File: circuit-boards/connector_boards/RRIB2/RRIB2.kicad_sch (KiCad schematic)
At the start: 90 parts, among them J1 DIO0, J10 DIO9, J11 DIO22, J12 DIO23, J13 DIO24, J14 DIO25, J15 RR_DIO0, J16 RR_DIO1, J17 RR_DIO2, J18 RR_DIO3, J19 RR_DIO4, J2 DIO1, J20 RR_DIO5, J21 RR_DIO6, J22 RR_DIO7, J23 RR_DIO8, J24 RR_DIO9, J25 ENC0, J26 ENC1, J27 ENC2, J28 ENC3, J29 ENC4, J3 DIO2, J30 ENC5, J31 ENC_AD0, J32 ENC_AD1, J33 ENC_AD2, J34 ENC_AD3, J35 ENC_AD4, J36 ENC_AD5, J37 RLY0, J38 RLY1, J39 RLY2, J4 DIO3, J40 RLY3, J41 AIN0, J42 AIN1, J43 AIN2, J44 AIN3, J45 AIN4, J46 AIN5, J47 AIN6, J48 AIN7, J49 RR_RELAY0, J5 DIO4, J50 RR_RELAY1, J51 RR_RELAY2, J52 RR_RELAY3, J53 RR_AIN0, J54 RR_AIN1, J55 RR_AIN2, J56 RR_AIN3, J57 PWM0, J58 PWM1, J59 PWM2, J6 DIO5, J60 PWM3, J61 PWM4, J62 PWM5, J63 PWM6, J64 PWM7, J65 PWM8, J66 PWM9, J67 RR_PWM0, J68 RR_PWM1, J69 RR_PWM2, J7 DIO6, J70 RR_PWM3, J71 RR_PWM4, J72 RR_PWM5, J73 RR_PWM6, J74 RR_PWM7, J75 RR_PWM8, J76 RR_PWM9, J77 RSL, J78 RS232, J79 I2C, J8 DIO7, J80 SPI0, J81 SPI1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

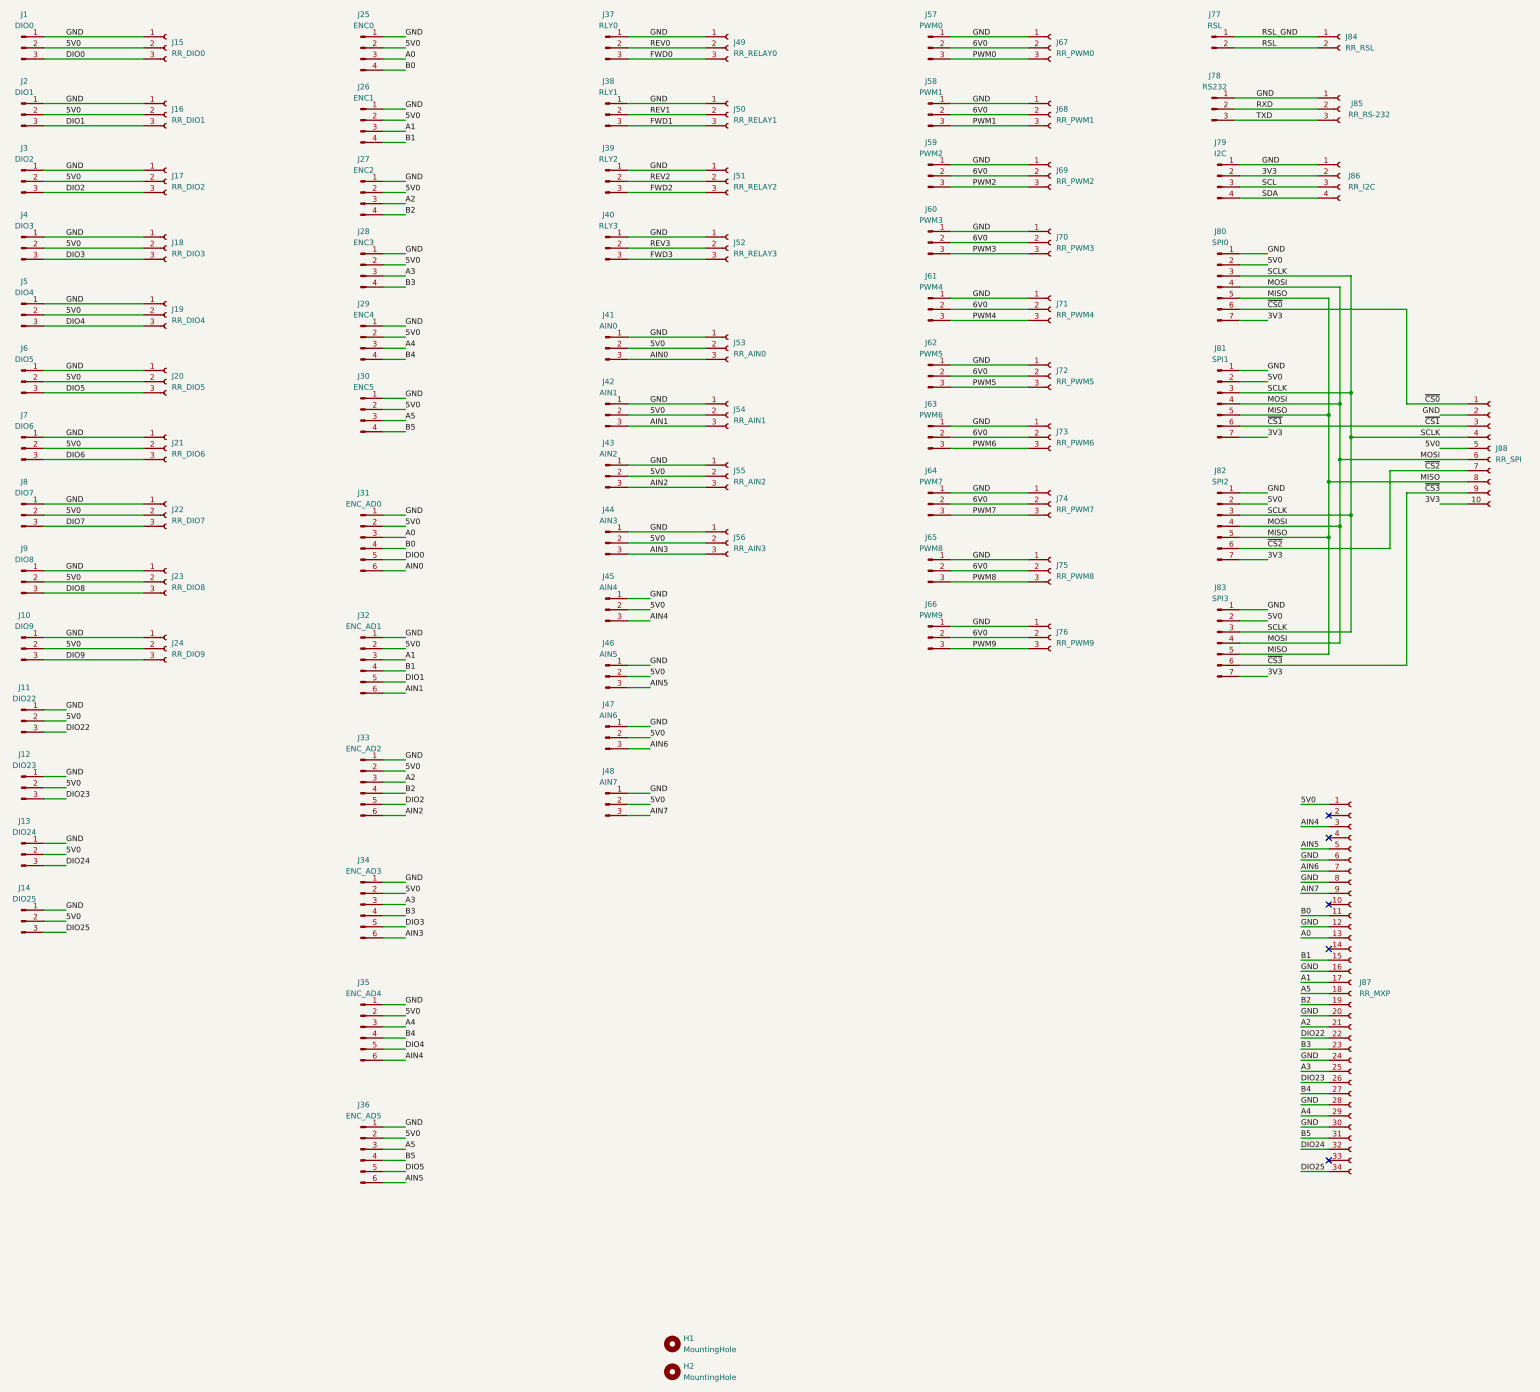
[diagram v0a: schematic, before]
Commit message: Updated boms and exported output files for connector boards
Signed-off-by: Scott <sgberman1@gmail.com>
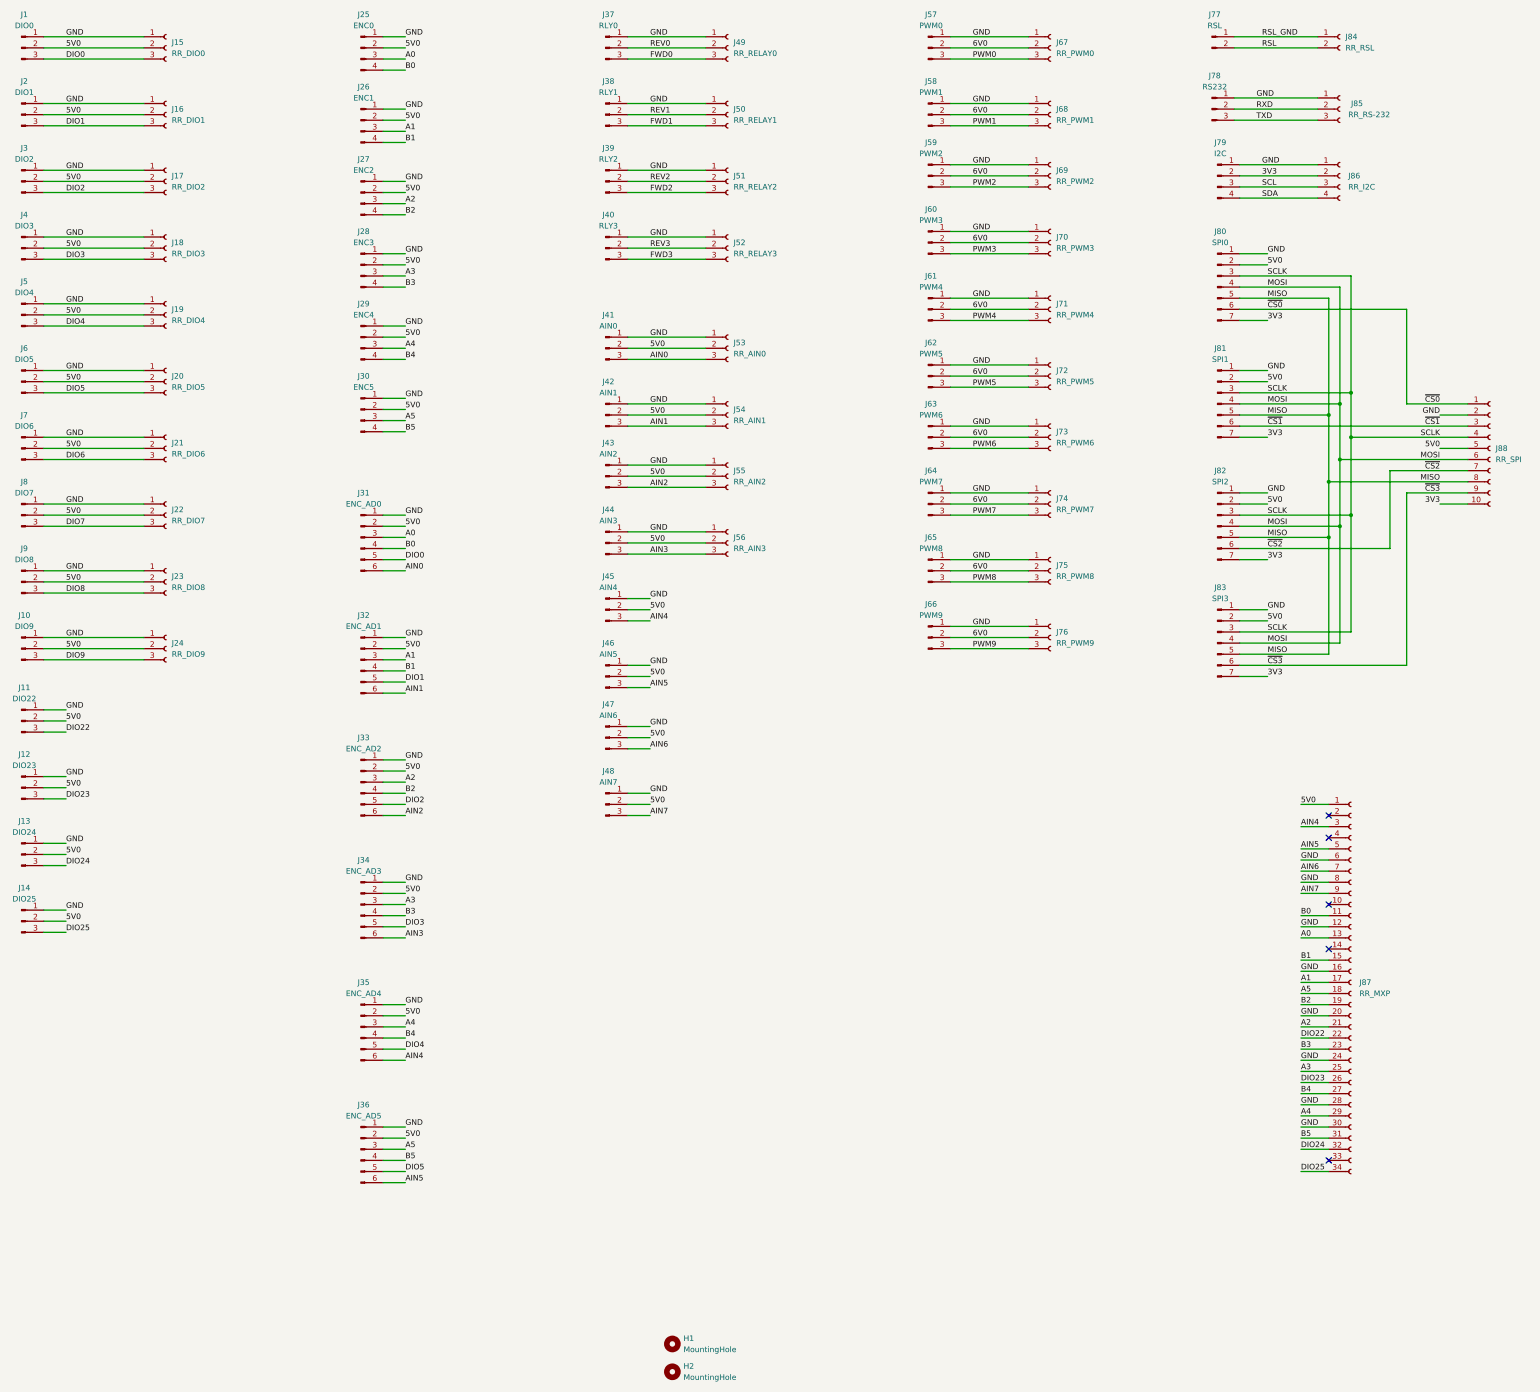
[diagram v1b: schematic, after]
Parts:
- J1, J10, J11, J12, J13, J14, J2, J3, J37, J38, J39, J4, J40, J41, J42, J43, J44, J45, J46, J47, J48, J5, J57, J58, J59, J6, J60, J61, J62, J63, J64, J65, J66, J7, J78, J8, J9: DIST (none) -> Digikey; DIST P/N (none) -> WM7991-ND; MFG P/N 70541-0002 -> 070541-0002
- J15, J16, J17, J18, J19, J20, J21, J22, J23, J24, J49, J50, J51, J52, J53, J54, J55, J56, J67, J68, J69, J70, J71, J72, J74, J75, J76, J85: DIST (none) -> Digikey; DIST P/N (none) -> S7001-ND
- J25, J26, J27, J28, J29, J30, J79: DIST (none) -> Digikey; DIST P/N (none) -> WM7992-ND; MFG P/N 70541-0003 -> 070541-0003
- J31, J32, J33, J34, J35, J36: DIST (none) -> Digikey; DIST P/N (none) -> WM20413-ND; MFG P/N 70541-0005 -> 070541-0005
- J73: DIST (none) -> Digikey; DIST P/N (none) -> S7001-ND; MFG Sullins Connector SolutionsSullins Connector Solutions -> Sullins Connector Solutions
- J77: DIST (none) -> Digikey; DIST P/N (none) -> WM14047-ND; MFG P/N 70541-0001 -> 070541-0001
- J80, J81, J82, J83: DIST (none) -> Digikey; DIST P/N (none) -> 0705410006-ND; MFG P/N 70541-0006 -> 070541-0006
- J84: DIST (none) -> Digikey; DIST P/N (none) -> S7000-ND
- J86: DIST (none) -> Digikey; DIST P/N (none) -> S7002-ND
- J87: DIST (none) -> Digikey; DIST P/N (none) -> S9199-ND
- J88: DIST (none) -> Digikey; DIST P/N (none) -> S9194-ND
